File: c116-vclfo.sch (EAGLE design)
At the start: 66 parts, among them U1 SCREW-M2X8, U10 FX2-20S-1.27DS, U11 ERM1-5MM, U2 SCREW-M2X8, U3 NUT-M2-SELFLOCK, U4 NUT-M2-SELFLOCK, U5 FX2-20P-1.27DS, U6 SCREW-M2X8, U7 SCREW-M2X8, U8 NUT-M2-SELFLOCK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

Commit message: C116 Update
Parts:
- removed VD1: BAT46, diodes-schottky:BAT46
- added O5, O7: 450-AA150(15MM,D,BLACK), hardware:450-AA150(15MM,D,BLACK)
- added O6, O8: 450-CP151(15MM,RED/WHITE), hardware:450-CP151(15MM,RED/WHITE)
- added R28, R31, R32: 100K(TH), resistors:100K(TH)
- added R29, R30: B100K(CD)(9MM), potentiometers:B100K(CD)(9MM)
- added R33, R34: 1K8(TH), resistors:1K8(TH)
- added SA5: MJS22R, switches:MJS22R
- DA2: value TL072IP -> TL074CN; device ic-ti:TL072IP -> ic-ti:TL074CN
- HL1: value YELLOW(2MMX5MM) -> RED/GREEN(2MMX5MM,BIPOLAR); device optoelectronics:YELLOW(2MMX5MM) -> optoelectronics:RED/GREEN(2MMX5MM,BIPOLAR)
- PCB1: device module-footprints:ST2-BOARD-50 -> module-footprints:ST2-BOARD-74
- R26, R27: value 1K8(TH) -> 100K(TH); device resistors:1K8(TH) -> resistors:100K(TH)
- SA3: value MHS233K -> MJS12R; device switches:MHS233K -> switches:MJS12R
- SA4: value MJS22R -> MHS233K; device switches:MJS22R -> switches:MHS233K
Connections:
- removed net N$39: DA3.4.IN+, SA3.1.CM, SA4.1.1, SA4.2.2
- new net N$37: R27.2, R30.W
- new net N$42: DA2.2.IN-, R28.1, R29.CW, R30.CW
- new net N$44: DA2.2.OUT, R28.2, R31.1
- new net N$45: DA2.3.IN-, R29.CCW, R30.CCW, R31.2, R32.1
- new net N$46: DA2.3.OUT, DA3.4.IN+, R32.2, SA5.1.1, SA5.2.2
- new net N$47: R27.1, SA3.CM
- new net N$48: R26.2, R29.W
- new net N$49: R26.1, SA4.1.CM
- net CV1_IN: now also SA3.2, SA5.2.1; no longer SA4.2.1
- net CV1_OUT: now also SA5.2.CM; no longer SA4.2.CM
- net CV2_IN: now also SA3.1, SA5.1.2; no longer SA4.1.2
- net CV2_OUT: now also SA5.1.CM; no longer SA4.1.CM
- net GND: now also DA2.3.IN+, DA2.4.IN+, R33.2; no longer R26.2
- net N$22: now also SA4.1.1; no longer SA3.1.1
- net N$29: now also SA4.1.2; no longer SA3.1.2
- net N$32: now also SA4.1.3; no longer SA3.1.3
- net N$36: now also R33.1, R34.2; no longer R26.1, R27.2
- net N$40: now also HL1.A, R34.1; no longer HL1.C, R27.1, VD1.A
- net N$41: now also HL1.C; no longer HL1.A, VD1.C
- net N$7: now also DA2.4.IN-; no longer DA2.2.IN-
- net N$8: now also DA2.4.OUT; no longer DA2.2.OUT
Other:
- moved on the sheet: DA2*, DA2.2, DA3*, DA3.4, R26, R27, U11

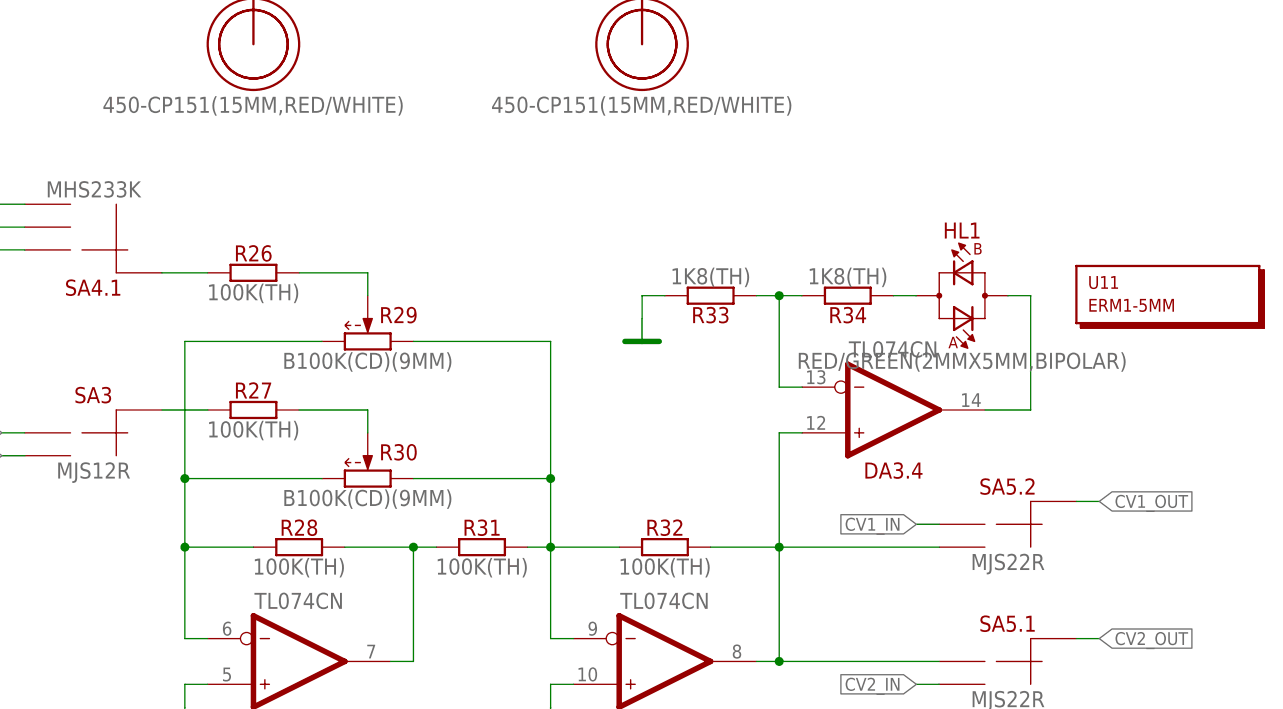
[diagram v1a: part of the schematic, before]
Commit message: C116 LED circuit update
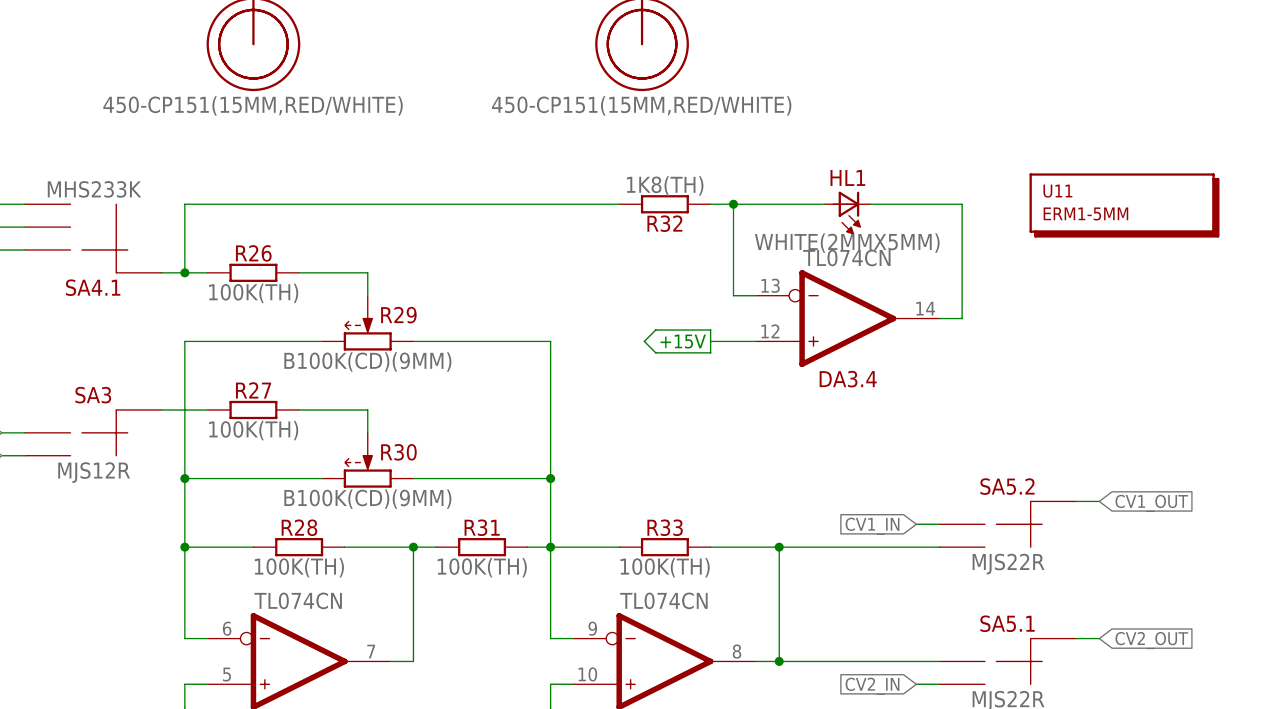
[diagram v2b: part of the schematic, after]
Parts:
- removed R34: 1K8(TH), resistors:1K8(TH)
- HL1: value RED/GREEN(2MMX5MM,BIPOLAR) -> WHITE(2MMX5MM); device optoelectronics:RED/GREEN(2MMX5MM,BIPOLAR) -> optoelectronics:WHITE(2MMX5MM)
- R32: value 100K(TH) -> 1K8(TH); device resistors:100K(TH) -> resistors:1K8(TH)
- R33: value 1K8(TH) -> 100K(TH); device resistors:1K8(TH) -> resistors:100K(TH)
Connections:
- removed net N$40: HL1.A, R34.1
- net +15V: now also DA3.4.IN+
- net GND: no longer R33.2
- net N$36: now also HL1.A, R32.1; no longer R33.1, R34.2
- net N$45: now also R33.1; no longer R32.1
- net N$46: now also R33.2; no longer DA3.4.IN+, R32.2
- net N$49: now also R32.2
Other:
- moved on the sheet: DA3.4, R32, R33, U11
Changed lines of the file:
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@@
 <part name="C5" library="capacitors-electrolytic" deviceset="?" device="10U/35V"/>
 <part name="C6" library="capacitors-electrolytic" deviceset="?" device="10U/35V"/>
-<part name="GND9" library="supply" deviceset="GND" device=""/>
-<part name="R33" library="resistors" deviceset="?" device="1K8(TH)"/>
-<part name="R34" library="resistors" deviceset="?" device="1K8(TH)"/>
+<part name="R32" library="resistors" deviceset="?" device="1K8(TH)"/>
 <part name="U11" library="hardware" deviceset="?" device="ERM1-5MM"/>
 <part name="SA3" library="switches" deviceset="MJS12R" device=""/>
 <part name="R27" library="resistors" deviceset="?" device="100K(TH)"/>
 <part name="R28" library="resistors" deviceset="?" device="100K(TH)"/>
-<part name="R32" library="resistors" deviceset="?" device="100K(TH)"/>
+<part name="R33" library="resistors" deviceset="?" device="100K(TH)"/>
 <part name="R31" library="resistors" deviceset="?" device="100K(TH)"/>
 <part name="GND7" library="supply" deviceset="GND" device=""/>
@@
 <part name="O7" library="hardware" deviceset="450-AA?" device="150(15MM,D,BLACK)"/>
 <part name="O8" library="hardware" deviceset="450-C?" device="P151(15MM,RED/WHITE)"/>
-<part name="HL1" library="optoelectronics" deviceset="?(2MMX5MM,BIPOLAR)" device="RED/GREEN"/>
 <part name="DA2" library="ic-ti" deviceset="TL074" device="CN"/>
+<part name="PWR15" library="supply" deviceset="+15V" device=""/>
+<part name="HL1" library="optoelectronics" deviceset="?(2MMX5MM)" device="WHITE"/>
 </parts>
 <sheets>
@@
 <instance part="DA3" gate=".2" x="220.98" y="-121.92" rot="MR180"/>
 <instance part="DA3" gate=".3" x="220.98" y="-160.02" rot="MR180"/>
-<instance part="DA3" gate=".4" x="340.36" y="-165.1" rot="MR180"/>
+<instance part="DA3" gate=".4" x="335.28" y="-154.94" rot="MR180"/>
 <instance part="R23" gate="G$1" x="220.98" y="-71.12"/>
 <instance part="R18" gate="G$1" x="200.66" y="-71.12"/>
@@
 <instance part="C5" gate="G$1" x="175.26" y="-33.02" rot="R270"/>
 <instance part="C6" gate="G$1" x="175.26" y="-43.18" rot="R270"/>
-<instance part="GND9" gate="VR1" x="312.42" y="-157.48"/>
-<instance part="R33" gate="G$1" x="320.04" y="-152.4" rot="R180"/>
-<instance part="R34" gate="G$1" x="335.28" y="-152.4" rot="R180"/>
-<instance part="U11" gate="G$1" x="370.84" y="-152.4"/>
+<instance part="R32" gate="G$1" x="314.96" y="-142.24" rot="R180"/>
+<instance part="U11" gate="G$1" x="365.76" y="-142.24"/>
 <instance part="SA3" gate="G$1" x="251.46" y="-167.64" rot="MR0"/>
 <instance part="R27" gate="G$1" x="269.24" y="-165.1"/>
 <instance part="R28" gate="G$1" x="274.32" y="-180.34"/>
-<instance part="R32" gate="G$1" x="314.96" y="-180.34"/>
+<instance part="R33" gate="G$1" x="314.96" y="-180.34"/>
 <instance part="R31" gate="G$1" x="294.64" y="-180.34"/>
 <instance part="GND7" gate="VR1" x="261.62" y="-200.66"/>
@@
 <instance part="O7" gate="G$1" x="312.42" y="-124.46"/>
 <instance part="O8" gate="G$1" x="312.42" y="-124.46"/>
-<instance part="HL1" gate="G$1" x="347.98" y="-152.4"/>
 <instance part="DA2" gate=".1" x="88.9" y="-119.38" rot="MR180"/>
 <instance part="DA2" gate=".4" x="129.54" y="-119.38" rot="MR180"/>
@@
 <instance part="DA2" gate=".3" x="314.96" y="-193.04" rot="MR180"/>
 <instance part="DA2" gate="*" x="226.06" y="-38.1"/>
+<instance part="PWR15" gate="G$1" x="320.04" y="-157.48" rot="R90"/>
+<instance part="HL1" gate="G$1" x="335.28" y="-142.24"/>
 </instances>
 <busses>
@@
 </segment>
 <segment>
-<pinref part="R33" gate="G$1" pin="2"/>
-<wire x1="314.96" y1="-152.4" x2="312.42" y2="-152.4" width="0.1524" layer="91"/>
-<pinref part="GND9" gate="VR1" pin="GND"/>
-<wire x1="312.42" y1="-152.4" x2="312.42" y2="-154.94" width="0.1524" layer="91"/>
-</segment>
-<segment>
 <pinref part="GND7" gate="VR1" pin="GND"/>
 <wire x1="264.16" y1="-195.58" x2="261.62" y2="-195.58" width="0.1524" layer="91"/>
@@
 <wire x1="195.58" y1="-147.32" x2="193.04" y2="-147.32" width="0.1524" layer="91"/>
 </segment>
+<segment>
+<pinref part="PWR15" gate="G$1" pin="+15V"/>
+<pinref part="DA3" gate=".4" pin="IN+"/>
+<wire x1="320.04" y1="-157.48" x2="325.12" y2="-157.48" width="0.1524" layer="91"/>
+</segment>
 </net>
 <net name="-15V" class="0">
@@
 <segment>
 <pinref part="DA3" gate=".4" pin="IN-"/>
-<wire x1="330.2" y1="-162.56" x2="327.66" y2="-162.56" width="0.1524" layer="91"/>
-<wire x1="327.66" y1="-162.56" x2="327.66" y2="-152.4" width="0.1524" layer="91"/>
-<pinref part="R33" gate="G$1" pin="1"/>
-<wire x1="327.66" y1="-152.4" x2="325.12" y2="-152.4" width="0.1524" layer="91"/>
-<pinref part="R34" gate="G$1" pin="2"/>
-<wire x1="330.2" y1="-152.4" x2="327.66" y2="-152.4" width="0.1524" layer="91"/>
-<junction x="327.66" y="-152.4"/>
+<wire x1="325.12" y1="-152.4" x2="322.58" y2="-152.4" width="0.1524" layer="91"/>
+<wire x1="322.58" y1="-152.4" x2="322.58" y2="-142.24" width="0.1524" layer="91"/>
+<pinref part="R32" gate="G$1" pin="1"/>
+<wire x1="322.58" y1="-142.24" x2="320.04" y2="-142.24" width="0.1524" layer="91"/>
+<junction x="322.58" y="-142.24"/>
+<pinref part="HL1" gate="G$1" pin="A"/>
+<wire x1="322.58" y1="-142.24" x2="332.74" y2="-142.24" width="0.1524" layer="91"/>
 </segment>
 </net>
 <net name="N$41" class="0">
 <segment>
-<wire x1="355.6" y1="-152.4" x2="355.6" y2="-165.1" width="0.1524" layer="91"/>
+<wire x1="347.98" y1="-142.24" x2="347.98" y2="-154.94" width="0.1524" layer="91"/>
 <pinref part="DA3" gate=".4" pin="OUT"/>
-<wire x1="355.6" y1="-165.1" x2="350.52" y2="-165.1" width="0.1524" layer="91"/>
+<wire x1="347.98" y1="-154.94" x2="345.44" y2="-154.94" width="0.1524" layer="91"/>
 <pinref part="HL1" gate="G$1" pin="C"/>
-<wire x1="353.06" y1="-152.4" x2="355.6" y2="-152.4" width="0.1524" layer="91"/>
+<wire x1="347.98" y1="-142.24" x2="337.82" y2="-142.24" width="0.1524" layer="91"/>
 </segment>
 </net>
@@
 <net name="N$45" class="0">
 <segment>
-<pinref part="R32" gate="G$1" pin="1"/>
+<pinref part="R33" gate="G$1" pin="1"/>
 <wire x1="309.88" y1="-180.34" x2="302.26" y2="-180.34" width="0.1524" layer="91"/>
 <wire x1="302.26" y1="-180.34" x2="302.26" y2="-190.5" width="0.1524" layer="91"/>
@@
 <net name="N$46" class="0">
 <segment>
-<pinref part="R32" gate="G$1" pin="2"/>
+<pinref part="R33" gate="G$1" pin="2"/>
 <wire x1="320.04" y1="-180.34" x2="327.66" y2="-180.34" width="0.1524" layer="91"/>
 <wire x1="327.66" y1="-180.34" x2="327.66" y2="-193.04" width="0.1524" layer="91"/>
@@
 <wire x1="345.44" y1="-193.04" x2="327.66" y2="-193.04" width="0.1524" layer="91"/>
 <junction x="327.66" y="-193.04"/>
-<pinref part="DA3" gate=".4" pin="IN+"/>
-<wire x1="330.2" y1="-167.64" x2="327.66" y2="-167.64" width="0.1524" layer="91"/>
-<wire x1="327.66" y1="-167.64" x2="327.66" y2="-180.34" width="0.1524" layer="91"/>
 <pinref part="DA2" gate=".3" pin="OUT"/>
 </segment>
@@
 </segment>
 </net>
-<net name="N$40" class="0">
-<segment>
-<pinref part="HL1" gate="G$1" pin="A"/>
-<pinref part="R34" gate="G$1" pin="1"/>
-<wire x1="342.9" y1="-152.4" x2="340.36" y2="-152.4" width="0.1524" layer="91"/>
-</segment>
-</net>
 <net name="N$49" class="0">
 <segment>
 <pinref part="SA4" gate=".1" pin="CM"/>
 <pinref part="R26" gate="G$1" pin="1"/>
-<wire x1="264.16" y1="-149.86" x2="259.08" y2="-149.86" width="0.1524" layer="91"/>
-</segment>
-</net>
+<wire x1="264.16" y1="-149.86" x2="261.62" y2="-149.86" width="0.1524" layer="91"/>
+<pinref part="R32" gate="G$1" pin="2"/>
+<wire x1="261.62" y1="-149.86" x2="259.08" y2="-149.86" width="0.1524" layer="91"/>
+<wire x1="309.88" y1="-142.24" x2="261.62" y2="-142.24" width="0.1524" layer="91"/>
+<wire x1="261.62" y1="-142.24" x2="261.62" y2="-149.86" width="0.1524" layer="91"/>
+<junction x="261.62" y="-149.86"/>
+</segment>
+</net>
